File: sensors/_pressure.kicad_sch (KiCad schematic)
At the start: 2 parts, among them U5 MS5611-01BA

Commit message: add Vref
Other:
- title: (none) -> PilotPi: Sensors
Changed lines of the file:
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@@
 	(generator_version "10.0")
 	(paper "A4")
+	(title_block
+		(title "PilotPi: Sensors")
+		(date "15 nov 2012")
+		(rev "4")
+	)
 	(junction
 		(at 118.11 85.09)

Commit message: added JP_VOLTS, Vref select jumper; VBAT_ADC Jumper
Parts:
- C11: Part (none) -> CC0402X7R50V104KN
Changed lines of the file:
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@@
 			)
 		)
-		(property "Part" ""
+		(property "Part" "CC0402X7R50V104KN"
 			(at 179.07 91.44 0)
 			(hide yes)

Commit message: use CLK out from CAN controller for UART (use 16 MHz instead of 14.7456MHz); minor changes
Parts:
- C11: value 100nF (104) 10% 16V -> 100nF 10% 16V
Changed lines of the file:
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@@
 			)
 		)
-		(property "Value" "100nF (104) 10% 16V"
+		(property "Value" "100nF 10% 16V"
 			(at 173.736 99.822 90)
 			(show_name no)

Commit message: use 2x8 for ADC header; added part numbers
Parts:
- U5: Part (none) -> MS561101BA03-50
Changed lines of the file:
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@@
+			)
+		)
+		(property "Part" "MS561101BA03-50"
+			(at 140.97 90.17 0)
+			(hide yes)
+			(show_name no)
+			(do_not_autoplace no)
+			(effects
+				(font
+					(size 1.27 1.27)
+				)
 			)
 		)

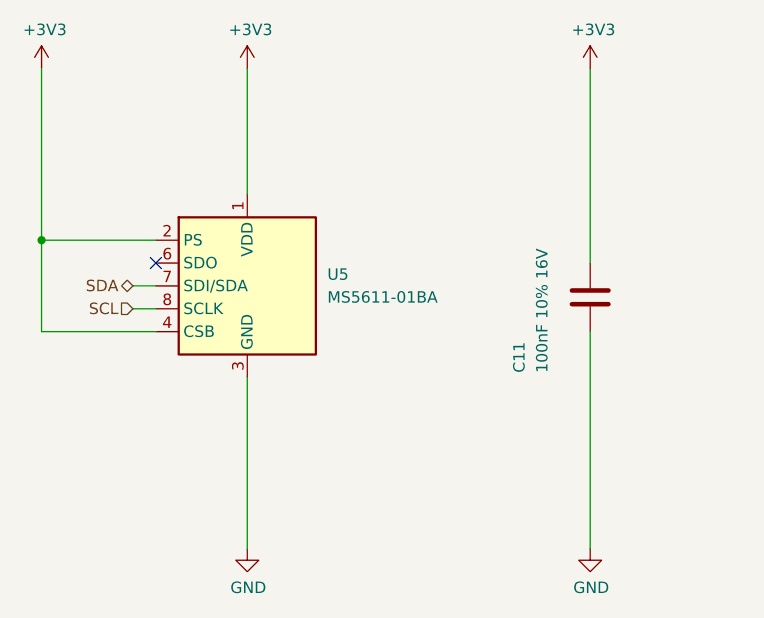
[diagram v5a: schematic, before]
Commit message: replace MS561101 pressure sensor with SPL06-001
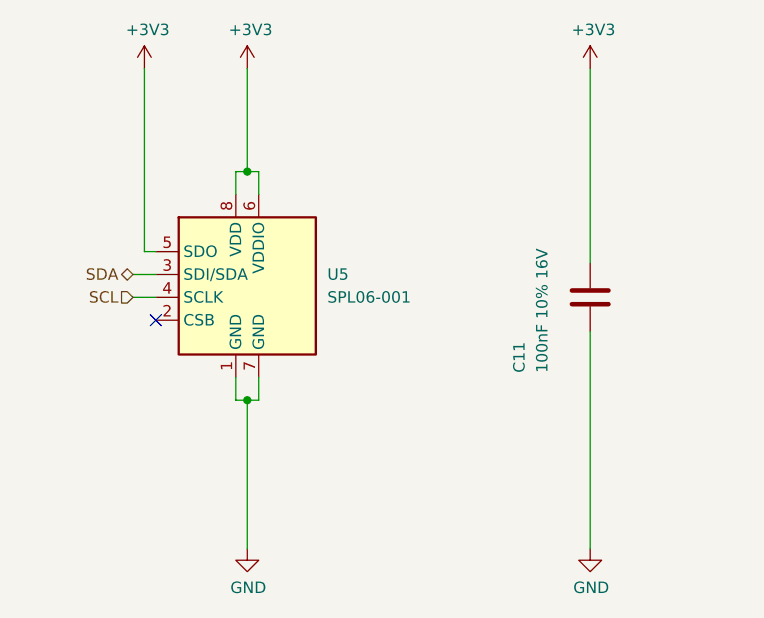
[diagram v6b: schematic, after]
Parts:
- C11: Part CC0402X7R50V104KN -> CL05B104KB54PNC
- U5: value MS5611-01BA -> SPL06-001; footprint Package_LGA:LGA-8_3x5mm_P1.25mm -> pilotpi:LGA-8_2.5x2mm_P0.65mm_ClockwisePinNumbering; symbol Sensor_Pressure:MS5611-01BA -> pilotpi:SPL06-001; Part MS561101BA03-50 -> SPL06-001
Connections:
- net +3V3: now also U5.6 (VDDIO), U5.8 (VDD); no longer U5.1 (VDD), U5.2 (PS), U5.4 (CSB)
- net GND: now also U5.1 (GND), U5.7 (GND); no longer U5.3 (GND)
- net SCL: now also U5.4 (SCLK); no longer U5.8 (SCLK)
- net SDA: now also U5.3 (SDI/SDA); no longer U5.7 (SDI/SDA)
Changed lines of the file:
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@@
 	)
 	(junction
-		(at 118.11 85.09)
+		(at 140.97 102.87)
 		(diameter 0)
 		(color 0 0 0 0)
 	)
+	(junction
+		(at 140.97 77.47)
+		(diameter 0)
+		(color 0 0 0 0)
+	)
 	(no_connect
-		(at 130.81 87.63)
-	)
-	(wire
-		(pts
-			(xy 118.11 85.09) (xy 130.81 85.09)
-		)
-		(stroke
-			(width 0)
-			(type default)
-		)
-	)
-	(wire
-		(pts
-			(xy 118.11 85.09) (xy 118.11 66.04)
-		)
-		(stroke
-			(width 0)
-			(type default)
-		)
-	)
-	(wire
-		(pts
-			(xy 128.27 90.17) (xy 130.81 90.17)
+		(at 130.81 93.98)
+	)
+	(wire
+		(pts
+			(xy 139.7 77.47) (xy 140.97 77.47)
+		)
+		(stroke
+			(width 0)
+			(type default)
+		)
+	)
+	(wire
+		(pts
+			(xy 142.24 102.87) (xy 140.97 102.87)
+		)
+		(stroke
+			(width 0)
+			(type default)
+		)
+	)
+	(wire
+		(pts
+			(xy 128.27 88.9) (xy 130.81 88.9)
 		)
 		(stroke
@@
 	(wire
 		(pts
-			(xy 130.81 95.25) (xy 118.11 95.25)
-		)
-		(stroke
-			(width 0)
-			(type default)
-		)
-	)
-	(wire
-		(pts
-			(xy 118.11 95.25) (xy 118.11 85.09)
-		)
-		(stroke
-			(width 0)
-			(type default)
-		)
-	)
-	(wire
-		(pts
-			(xy 128.27 92.71) (xy 130.81 92.71)
-		)
-		(stroke
-			(width 0)
-			(type default)
-		)
-	)
-	(wire
-		(pts
-			(xy 140.97 66.04) (xy 140.97 80.01)
-		)
-		(stroke
-			(width 0)
-			(type default)
-		)
-	)
-	(wire
-		(pts
-			(xy 140.97 100.33) (xy 140.97 119.38)
+			(xy 139.7 100.33) (xy 139.7 102.87)
+		)
+		(stroke
+			(width 0)
+			(type default)
+		)
+	)
+	(wire
+		(pts
+			(xy 139.7 80.01) (xy 139.7 77.47)
+		)
+		(stroke
+			(width 0)
+			(type default)
+		)
+	)
+	(wire
+		(pts
+			(xy 139.7 102.87) (xy 140.97 102.87)
+		)
+		(stroke
+			(width 0)
+			(type default)
+		)
+	)
+	(wire
+		(pts
+			(xy 142.24 80.01) (xy 142.24 77.47)
+		)
+		(stroke
+			(width 0)
+			(type default)
+		)
+	)
+	(wire
+		(pts
+			(xy 128.27 91.44) (xy 130.81 91.44)
+		)
+		(stroke
+			(width 0)
+			(type default)
+		)
+	)
+	(wire
+		(pts
+			(xy 129.54 86.36) (xy 129.54 66.04)
+		)
+		(stroke
+			(width 0)
+			(type default)
+		)
+	)
+	(wire
+		(pts
+			(xy 142.24 77.47) (xy 140.97 77.47)
+		)
+		(stroke
+			(width 0)
+			(type default)
+		)
+	)
+	(wire
+		(pts
+			(xy 130.81 86.36) (xy 129.54 86.36)
+		)
+		(stroke
+			(width 0)
+			(type default)
+		)
+	)
+	(wire
+		(pts
+			(xy 140.97 66.04) (xy 140.97 77.47)
+		)
+		(stroke
+			(width 0)
+			(type default)
+		)
+	)
+	(wire
+		(pts
+			(xy 142.24 100.33) (xy 142.24 102.87)
+		)
+		(stroke
+			(width 0)
+			(type default)
+		)
+	)
+	(wire
+		(pts
+			(xy 140.97 102.87) (xy 140.97 119.38)
 		)
 		(stroke
@@
 	(hierarchical_label "SDA"
 		(shape bidirectional)
-		(at 128.27 90.17 180)
+		(at 128.27 88.9 180)
 		(effects
 			(font
@@
 	(hierarchical_label "SCL"
 		(shape input)
-		(at 128.27 92.71 180)
+		(at 128.27 91.44 180)
 		(effects
 			(font
@@
 	)
 	(symbol
-		(lib_id "Sensor_Pressure:MS5611-01BA")
+		(lib_id "pilotpi:SPL06-001")
 		(at 140.97 90.17 0)
 		(unit 1)
@@
 			)
 		)
-		(property "Value" "MS5611-01BA"
+		(property "Value" "SPL06-001"
 			(at 149.86 91.4399 0)
 			(show_name no)
@@
 			)
 		)
-		(property "Footprint" "Package_LGA:LGA-8_3x5mm_P1.25mm"
+		(property "Footprint" "pilotpi:LGA-8_2.5x2mm_P0.65mm_ClockwisePinNumbering"
 			(at 140.97 90.17 0)
 			(hide yes)
@@
 			)
 		)
-		(property "Datasheet" "https://www.te.com/commerce/DocumentDelivery/DDEController?Action=srchrtrv&DocNm=MS5611-01BA03&DocType=Data+Sheet&DocLang=English"
+		(property "Datasheet" "https://www.te.com/commerce/DocumentDelivery/DDEController?Action=showdoc&DocId=Data+Sheet%7FMS5607-02BA03%7FB2%7Fpdf%7FEnglish%7FENG_DS_MS5607-02BA03_B2.pdf%7FCAT-BLPS0035"
 			(at 140.97 90.17 0)
 			(hide yes)
@@
 			)
 		)
-		(property "Description" "Barometric pressure sensor, 10cm resolution, 10 to 1200 mbar, I2C and SPI interface up to 20MHz, LGA-8"
+		(property "Description" "Barometric pressure sensor, 20cm resolution, 10 to 1200 mbar, I2C and SPI interface up to 20MHz, LGA-8"
 			(at 140.97 90.17 0)
 			(hide yes)
@@
 			)
 		)
-		(property "Part" "MS561101BA03-50"
+		(property "Part" "SPL06-001"
 			(at 140.97 90.17 0)
 			(hide yes)
@@
 	(symbol
 		(lib_id "power:+3.3V")
-		(at 118.11 66.04 0)
+		(at 129.54 66.04 0)
 		(unit 1)
 		(body_style 1)
@@
 		(dnp no)
 		(property "Reference" "#PWR053"
-			(at 118.11 69.85 0)
+			(at 129.54 69.85 0)
 			(hide yes)
 			(show_name no)
@@
 		)
 		(property "Value" "+3V3"
-			(at 118.4783 61.7156 0)
+			(at 129.9083 61.7156 0)
 			(show_name no)
 			(do_not_autoplace no)
@@
 		)
 		(property "Footprint" ""
-			(at 118.11 66.04 0)
+			(at 129.54 66.04 0)
 			(show_name no)
 			(do_not_autoplace no)
@@
 		)
 		(property "Datasheet" ""
-			(at 118.11 66.04 0)
+			(at 129.54 66.04 0)
 			(show_name no)
 			(do_not_autoplace no)
@@
 		)
 		(property "Description" "Power symbol creates a global label with name \"+3.3V\""
-			(at 118.11 66.04 0)
+			(at 129.54 66.04 0)
 			(hide yes)
 			(show_name no)
@@
 			)
 		)
-		(property "Part" "CC0402X7R50V104KN"
+		(property "Part" "CL05B104KB54PNC"
 			(at 179.07 91.44 0)
 			(hide yes)

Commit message: use series resistor for external clk; add 1uF caps
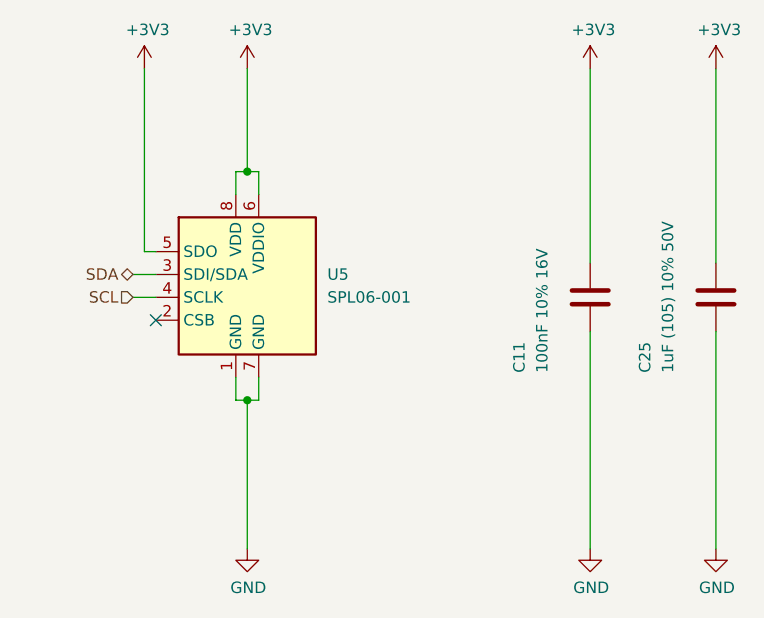
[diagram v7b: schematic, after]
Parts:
- added C25: 1uF (105) 10% 50V, Capacitor_SMD:C_0603_1608Metric, symbol Device:C
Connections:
- net +3V3: now also C25.1
- net GND: now also C25.2
